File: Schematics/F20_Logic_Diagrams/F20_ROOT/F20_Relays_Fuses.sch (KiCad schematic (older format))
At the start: 18 parts

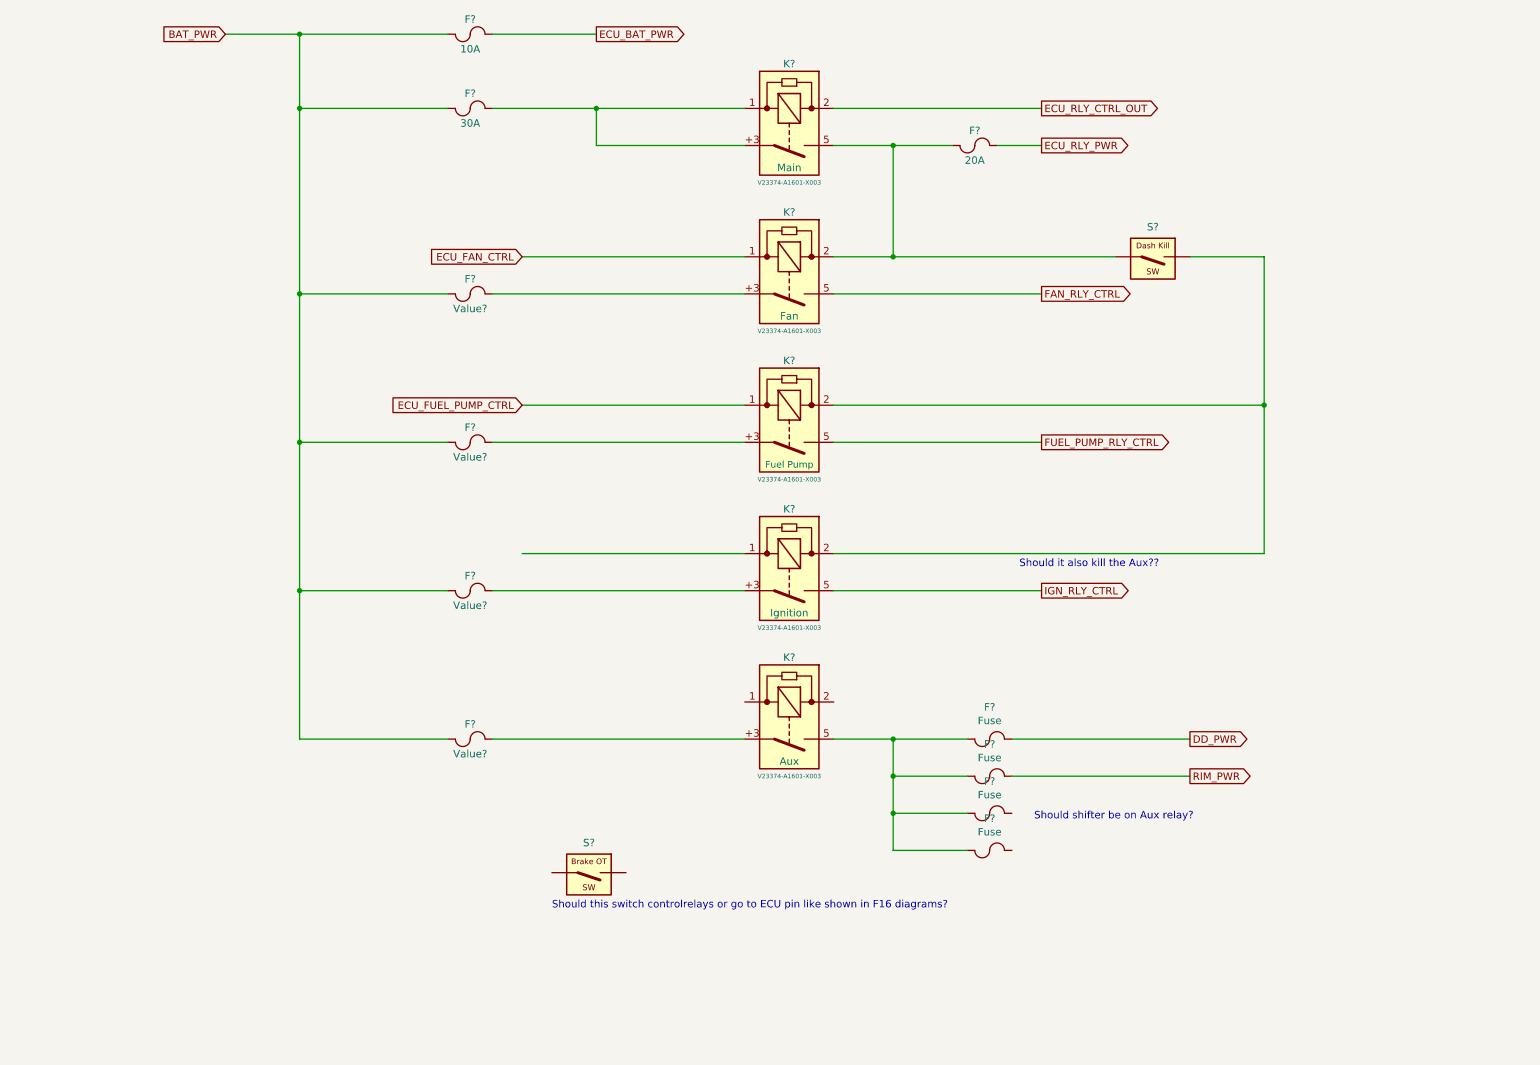
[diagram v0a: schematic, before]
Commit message: Updated per AD commit. O2 sensor schematic, transponder schematic.
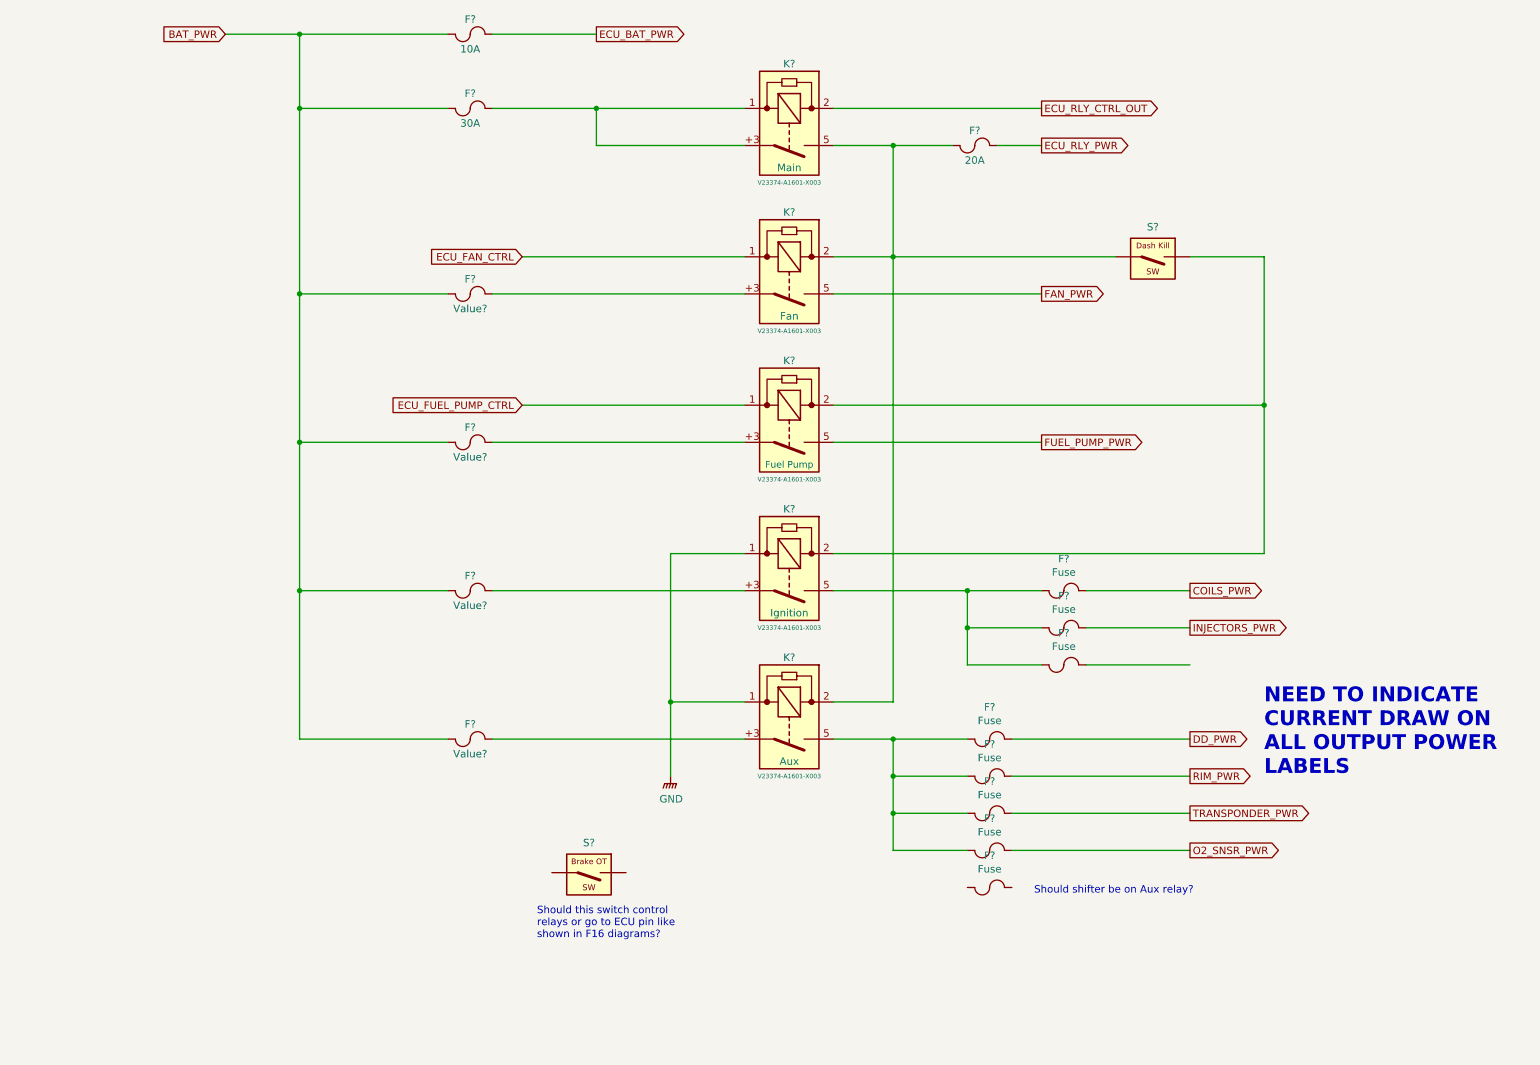
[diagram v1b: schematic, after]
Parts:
- added F? (x4): Fuse, symbol FSAE_Library:Fuse
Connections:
- net at F?.1, K?.2, K?.5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: now also K?.2
- net GNDPWR: now reaches K?.1
- net GNDPWR: now also K?.1
- net TRANSPONDER_PWR: now reaches F?.2
- net O2_SNSR_PWR: now reaches F?.2
- net FAN_RLY_CTRL renamed FAN_PWR
- net FUEL_PUMP_RLY_CTRL renamed FUEL_PUMP_PWR
- net IGN_RLY_CTRL: no longer names the net of K?.5
- net IGN_RLY_CTRL: now also F?.1, F?.1, F?.1
- new net COILS_PWR: F?.2
- new net INJECTORS_PWR: F?.2
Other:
- note added: "NEED TO INDICATE\nCURRENT DRAW ON\nALL OUTPUT POWER\nLABELS"
- note added: "Should this switch control\nrelays or go to ECU pin like\nshown in F16 diagrams?"
- note removed: "Should it also kill the Aux??"
- note removed: "Should this switch controlrelays or go to ECU pin like shown in F16 diagrams?"
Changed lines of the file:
@@
 EESchema Schematic File Version 4
-LIBS:F20_ROOT-cache
 EELAYER 30 0
 EELAYER END
 $Descr A 11000 8500
 encoding utf-8
-Sheet 7 7
+Sheet 8 9
 Title "Relays and Fuses"
 Date "2020-01-29"
@@
 	9000 4500 6100 4500
 Connection ~ 9000 3500
-Text Notes 7350 4600 0    50   ~ 0
-Should it also kill the Aux??
 $Comp
 L FSAE_Library:Bake_OT_SW S?
@@
 	1    0    0    -1
 $EndComp
-Text Notes 4200 6900 0    50   ~ 0
-Should this switch controlrelays or go to ECU pin like shown in F16 diagrams?
+Text Notes 4100 7100 0    50   ~ 0
+Should this switch control\nrelays or go to ECU pin like\nshown in F16 diagrams?
 Text GLabel 2000 1000 0    50   Input ~ 0
 BAT_PWR
@@
 	7500 2750 6100 2750
 Text GLabel 7500 3750 2    50   Output ~ 0
-FUEL_PUMP_RLY_CTRL
+FUEL_PUMP_PWR
 Wire Wire Line
 	7500 3750 6100 3750
@@
 	4000 3500 5500 3500
 Wire Wire Line
-	5500 4500 4000 4500
-Wire Wire Line
-	6100 4750 7500 4750
+	5500 4500 5000 4500
+Wire Wire Line
+	6100 4750 7000 4750
 $Comp
 L FSAE_Library:Fuse F?
@@
 Text GLabel 8500 5750 2    50   Output ~ 0
 DD_PWR
-Text GLabel 7500 4750 2    50   Output ~ 0
-IGN_RLY_CTRL
 Text GLabel 8500 6000 2    50   Output ~ 0
 RIM_PWR
 Wire Wire Line
 	8500 6000 7300 6000
-Text Notes 7450 6300 0    50   ~ 0
+Text Notes 7450 6800 0    50   ~ 0
 Should shifter be on Aux relay?
 $Comp
@@
 Wire Wire Line
 	9000 2500 9000 3500
+Wire Wire Line
+	6500 2500 6500 5500
+Wire Wire Line
+	6500 5500 6100 5500
+$Comp
+L FSAE_Library:Fuse F?
+U 1 1 5E3A862B
+P 7500 5000
+F 0 "F?" H 7650 5215 50  0000 C CNN
+F 1 "Fuse" H 7650 5124 50  0000 C CNN
+F 2 "" H 7650 5080 50  0001 C CNN
+F 3 "~" V 7650 5150 50  0001 C CNN
+	1    7500 5000
+	1    0    0    -1
+$EndComp
+Wire Wire Line
+	7000 4750 7000 5000
+Wire Wire Line
+	7000 5000 7500 5000
+Wire Wire Line
+	7800 5000 8500 5000
+Text GLabel 8500 6500 2    50   Output ~ 0
+O2_SNSR_PWR
+Text Notes 9000 6000 0    100  ~ 20
+NEED TO INDICATE\nCURRENT DRAW ON\nALL OUTPUT POWER\nLABELS
+$Comp
+L FSAE_Library:Fuse F?
+U 1 1 5E3C06C7
+P 7000 6750
+F 0 "F?" H 7150 6965 50  0000 C CNN
+F 1 "Fuse" H 7150 6874 50  0000 C CNN
+F 2 "" H 7150 6830 50  0001 C CNN
+F 3 "~" V 7150 6900 50  0001 C CNN
+	1    7000 6750
+	1    0    0    -1
+$EndComp
+$Comp
+L FSAE_Library:GND #PWR?
+U 1 1 5E3C4736
+P 5000 6000
+F 0 "#PWR?" H 5000 5800 50  0001 C CNN
+F 1 "GND" H 5004 5846 50  0000 C CNN
+F 2 "" H 5000 5950 50  0001 C CNN
+F 3 "" H 5000 5950 50  0001 C CNN
+	1    5000 6000
+	1    0    0    -1
+$EndComp
+Wire Wire Line
+	5000 6000 5000 5500
+Wire Wire Line
+	5000 5500 5500 5500
+Wire Wire Line
+	5000 4500 5000 5500
+Connection ~ 5000 5500
+Wire Wire Line
+	7300 6250 8500 6250
+Text GLabel 8500 6250 2    50   Output ~ 0
+TRANSPONDER_PWR
 Text GLabel 7500 2750 2    50   Output ~ 0
-FAN_RLY_CTRL
+FAN_PWR
+$Comp
+L FSAE_Library:Fuse F?
+U 1 1 5E3D8B35
+P 7500 5250
+F 0 "F?" H 7650 5465 50  0000 C CNN
+F 1 "Fuse" H 7650 5374 50  0000 C CNN
+F 2 "" H 7650 5330 50  0001 C CNN
+F 3 "~" V 7650 5400 50  0001 C CNN
+	1    7500 5250
+	1    0    0    -1
+$EndComp
+Wire Wire Line
+	7500 5250 7000 5250
+Wire Wire Line
+	7000 5250 7000 5000
+Connection ~ 7000 5000
+Wire Wire Line
+	7300 6500 8500 6500
+Wire Wire Line
+	7800 5250 8500 5250
+$Comp
+L FSAE_Library:Fuse F?
+U 1 1 5E3E67D5
+P 7500 4750
+F 0 "F?" H 7650 4965 50  0000 C CNN
+F 1 "Fuse" H 7650 4874 50  0000 C CNN
+F 2 "" H 7650 4830 50  0001 C CNN
+F 3 "~" V 7650 4900 50  0001 C CNN
+	1    7500 4750
+	1    0    0    -1
+$EndComp
+Wire Wire Line
+	7000 4750 7500 4750
+Connection ~ 7000 4750
+Wire Wire Line
+	7800 4750 8500 4750
+Text GLabel 8500 4750 2    50   Output ~ 0
+COILS_PWR
+Text GLabel 8500 5000 2    50   Output ~ 0
+INJECTORS_PWR
 $EndSCHEMATC

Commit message: Weekly update. Added Tire temp sensors drawing.
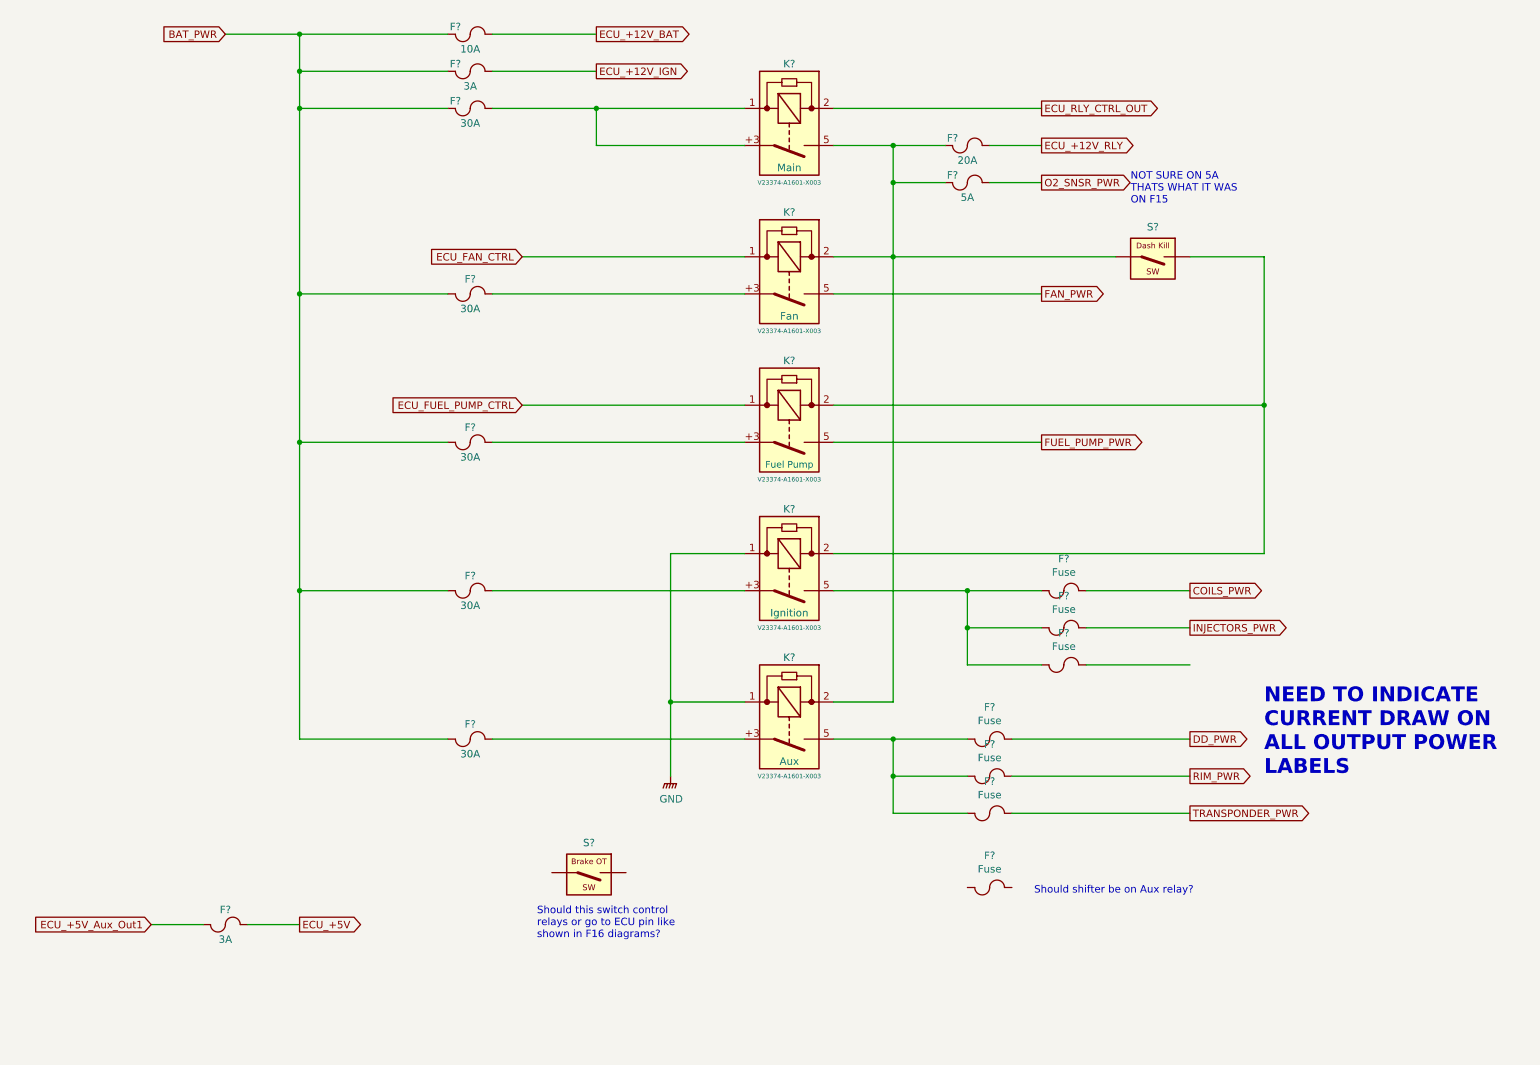
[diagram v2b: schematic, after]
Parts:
- removed F?: Fuse, symbol FSAE_Library:Fuse
- added F? (x2): 3A, symbol FSAE_Library:Fuse
- added F?: 5A, symbol FSAE_Library:Fuse
- F? (x4): value Value? -> 30A
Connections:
- net BAT_PWR: now also F?.1
- net O2_SNSR_PWR: now also F?.2
- net at F?.1, K?.2, K?.2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: now also F?.1
- net ECU_BAT_PWR renamed ECU_+12V_BAT
- net ECU_RLY_PWR renamed ECU_+12V_RLY
- new net ECU_+12V_IGN: F?.2
- new net ECU_+5V: F?.2
- new net ECU_+5V_Aux_Out1: F?.1
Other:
- note added: "NOT SURE ON 5A\nTHATS WHAT IT WAS\nON F15"
- moved on the sheet: F?
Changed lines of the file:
@@
 EESchema Schematic File Version 4
+LIBS:F20_ROOT-cache
 EELAYER 30 0
 EELAYER END
 $Descr A 11000 8500
 encoding utf-8
-Sheet 8 9
+Sheet 9 11
 Title "Relays and Fuses"
 Date "2020-01-29"
@@
 P 3500 2750
 F 0 "F?" H 3650 2850 50  0000 C CNN
-F 1 "Value?" H 3650 2650 50  0000 C CNN
+F 1 "30A" H 3650 2650 50  0000 C CNN
 F 2 "" H 3650 2830 50  0001 C CNN
 F 3 "~" V 3650 2900 50  0001 C CNN
@@
 P 3500 3750
 F 0 "F?" H 3650 3850 50  0000 C CNN
-F 1 "Value?" H 3650 3650 50  0000 C CNN
+F 1 "30A" H 3650 3650 50  0000 C CNN
 F 2 "" H 3650 3830 50  0001 C CNN
 F 3 "~" V 3650 3900 50  0001 C CNN
@@
 P 3500 4750
 F 0 "F?" H 3650 4850 50  0000 C CNN
-F 1 "Value?" H 3650 4650 50  0000 C CNN
+F 1 "30A" H 3650 4650 50  0000 C CNN
 F 2 "" H 3650 4830 50  0001 C CNN
 F 3 "~" V 3650 4900 50  0001 C CNN
@@
 P 3500 5750
 F 0 "F?" H 3650 5850 50  0000 C CNN
-F 1 "Value?" H 3650 5650 50  0000 C CNN
+F 1 "30A" H 3650 5650 50  0000 C CNN
 F 2 "" H 3650 5830 50  0001 C CNN
 F 3 "~" V 3650 5900 50  0001 C CNN
@@
 	1    0    0    -1
 $EndComp
-$Comp
-L FSAE_Library:Fuse F?
-U 1 1 5E3E1BF4
-P 7000 6500
-F 0 "F?" H 7150 6715 50  0000 C CNN
-F 1 "Fuse" H 7150 6624 50  0000 C CNN
-F 2 "" H 7150 6580 50  0001 C CNN
-F 3 "~" V 7150 6650 50  0001 C CNN
-	1    7000 6500
-	1    0    0    -1
-$EndComp
 Wire Wire Line
 	6100 5750 6500 5750
@@
 Wire Wire Line
 	6500 6000 7000 6000
-Wire Wire Line
-	6500 6250 6500 6500
-Wire Wire Line
-	6500 6500 7000 6500
-Connection ~ 6500 6250
 Wire Wire Line
 	7300 5750 8500 5750
@@
 U 1 1 5E401951
 P 3500 1000
-F 0 "F?" H 3650 1100 50  0000 C CNN
+F 0 "F?" H 3550 1050 50  0000 C CNN
 F 1 "10A" H 3650 900 50  0000 C CNN
 F 2 "" H 3650 1080 50  0001 C CNN
@@
 	2500 1000 3500 1000
 Text GLabel 4500 1000 2    50   Output ~ 0
-ECU_BAT_PWR
+ECU_+12V_BAT
 Wire Wire Line
 	3800 1000 4500 1000
-Wire Wire Line
-	2500 1000 2500 1500
 $Comp
 L FSAE_Library:Fuse F?
 U 1 1 5E40775B
 P 3500 1500
-F 0 "F?" H 3650 1600 50  0000 C CNN
+F 0 "F?" H 3550 1550 50  0000 C CNN
 F 1 "30A" H 3650 1400 50  0000 C CNN
 F 2 "" H 3650 1580 50  0001 C CNN
@@
 ECU_FAN_CTRL
 Text GLabel 7500 1750 2    50   Output ~ 0
-ECU_RLY_PWR
+ECU_+12V_RLY
 $Comp
 L FSAE_Library:Fuse F?
 U 1 1 5E442A66
-P 6900 1750
-F 0 "F?" H 7050 1850 50  0000 C CNN
-F 1 "20A" H 7050 1650 50  0000 C CNN
-F 2 "" H 7050 1830 50  0001 C CNN
-F 3 "~" V 7050 1900 50  0001 C CNN
-	1    6900 1750
-	1    0    0    -1
-$EndComp
-Wire Wire Line
-	7200 1750 7500 1750
+P 6850 1750
+F 0 "F?" H 6900 1800 50  0000 C CNN
+F 1 "20A" H 7000 1650 50  0000 C CNN
+F 2 "" H 7000 1830 50  0001 C CNN
+F 3 "~" V 7000 1900 50  0001 C CNN
+	1    6850 1750
+	1    0    0    -1
+$EndComp
 Wire Wire Line
 	6100 1750 6500 1750
-Wire Wire Line
-	6500 1750 6500 2500
 Wire Wire Line
 	6500 2500 6100 2500
 Connection ~ 6500 1750
 Wire Wire Line
-	6500 1750 6900 1750
+	6500 1750 6850 1750
 Connection ~ 6500 2500
 Wire Wire Line
@@
 Wire Wire Line
 	7800 5000 8500 5000
-Text GLabel 8500 6500 2    50   Output ~ 0
+Text GLabel 7500 2000 2    50   Output ~ 0
 O2_SNSR_PWR
 Text Notes 9000 6000 0    100  ~ 20
@@
 $EndComp
 $Comp
-L FSAE_Library:GND #PWR?
+L FSAE_Library:GND #PWR0111
 U 1 1 5E3C4736
 P 5000 6000
-F 0 "#PWR?" H 5000 5800 50  0001 C CNN
+F 0 "#PWR0111" H 5000 5800 50  0001 C CNN
 F 1 "GND" H 5004 5846 50  0000 C CNN
 F 2 "" H 5000 5950 50  0001 C CNN
@@
 Connection ~ 7000 5000
 Wire Wire Line
-	7300 6500 8500 6500
-Wire Wire Line
 	7800 5250 8500 5250
 $Comp
@@
 Text GLabel 8500 5000 2    50   Output ~ 0
 INJECTORS_PWR
+Text GLabel 1500 7000 0    50   Input ~ 0
+ECU_+5V_Aux_Out1
+$Comp
+L FSAE_Library:Fuse F?
+U 1 1 5E3EDD00
+P 1850 7000
+F 0 "F?" H 2000 7100 50  0000 C CNN
+F 1 "3A" H 2000 6900 50  0000 C CNN
+F 2 "" H 2000 7080 50  0001 C CNN
+F 3 "~" V 2000 7150 50  0001 C CNN
+	1    1850 7000
+	1    0    0    -1
+$EndComp
+Wire Wire Line
+	1850 7000 1500 7000
+Wire Wire Line
+	2150 7000 2500 7000
+Text GLabel 2500 7000 2    50   Output ~ 0
+ECU_+5V
+Wire Wire Line
+	2500 1000 2500 1250
+Wire Wire Line
+	6500 1750 6500 2000
+$Comp
+L FSAE_Library:Fuse F?
+U 1 1 5E471A10
+P 6850 2000
+F 0 "F?" H 6900 2050 50  0000 C CNN
+F 1 "5A" H 7000 1900 50  0000 C CNN
+F 2 "" H 7000 2080 50  0001 C CNN
+F 3 "~" V 7000 2150 50  0001 C CNN
+	1    6850 2000
+	1    0    0    -1
+$EndComp
+Wire Wire Line
+	6850 2000 6500 2000
+Connection ~ 6500 2000
+Wire Wire Line
+	6500 2000 6500 2500
+Wire Wire Line
+	7150 2000 7500 2000
+Wire Wire Line
+	7150 1750 7500 1750
+Text Notes 8100 2150 0    50   ~ 0
+NOT SURE ON 5A\nTHATS WHAT IT WAS\nON F15
+$Comp
+L FSAE_Library:Fuse F?
+U 1 1 5E480F23
+P 3500 1250
+F 0 "F?" H 3550 1300 50  0000 C CNN
+F 1 "3A" H 3650 1150 50  0000 C CNN
+F 2 "" H 3650 1330 50  0001 C CNN
+F 3 "~" V 3650 1400 50  0001 C CNN
+	1    3500 1250
+	1    0    0    -1
+$EndComp
+Wire Wire Line
+	3500 1250 2500 1250
+Connection ~ 2500 1250
+Wire Wire Line
+	2500 1250 2500 1500
+Wire Wire Line
+	3800 1250 4500 1250
+Text GLabel 4500 1250 2    50   Output ~ 0
+ECU_+12V_IGN
 $EndSCHEMATC

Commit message: 02/18/20 update
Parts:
- F14, F15, F16: renamed from F?; value Fuse -> 1A
- gave numbers to parts that had none: 21
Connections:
- net at K3.2, K4.2: now also S3.~; no longer S2.~
- net at F14.1, F15.1, F16.1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: now also F17.1
- net at S3.~: now also S2.~
- net ECU_+5V renamed ECU_+5V_1
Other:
- note added: "* Driver Display (1A)\n* Brake Pressure sensors (40mAx2 -> 100mA)"
- note added: "KA7805 voltage regulator (1A)"
- note added: "MUST KILL IGNITION AND\nFUEL PER FSAE RULES"
- note added: "Recommended 1A supply (500mA min for stability)"
- note added: "about 60mA"
- note removed: "Should shifter be on Aux relay?"
- note removed: "Should this switch control\nrelays or go to ECU pin like\nshown in F16 diagrams?"
- moved on the sheet: F10, F11, F12, F13, F17, F18, F2, F3, F4, F5, F6, F7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

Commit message: 02/19/20 update
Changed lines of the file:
@@
 Text GLabel 8000 2000 2    50   Output ~ 0
 O2_SNSR_PWR
-Text Notes 8700 4350 0    100  ~ 20
+Text Notes 8850 4450 0    100  ~ 20
 NEED TO INDICATE\nCURRENT DRAW ON\nALL OUTPUT POWER\nLABELS
 $Comp

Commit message: Added injectors drawing
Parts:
- removed F12: Fuse, symbol FSAE_Library:Fuse
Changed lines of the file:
@@
 $Descr A 11000 8500
 encoding utf-8
-Sheet 10 13
+Sheet 11 14
 Title "Relays and Fuses"
 Date "2020-01-29"
@@
 FAN_PWR
 $Comp
-L FSAE_Library:Fuse F12
-U 1 1 5E3D8B35
-P 7000 5250
-F 0 "F12" H 7300 5300 50  0000 C CNN
-F 1 "Fuse" H 7300 5200 50  0000 C CNN
-F 2 "" H 7150 5330 50  0001 C CNN
-F 3 "~" V 7150 5400 50  0001 C CNN
-	1    7000 5250
-	1    0    0    -1
-$EndComp
-Wire Wire Line
-	7000 5250 6500 5250
-Wire Wire Line
-	6500 5250 6500 5000
-Connection ~ 6500 5000
-Wire Wire Line
-	7300 5250 8000 5250
-$Comp
 L FSAE_Library:Fuse F10
